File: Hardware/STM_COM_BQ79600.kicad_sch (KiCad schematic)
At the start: 8 parts, among them U3 PBQ79600PWQ1

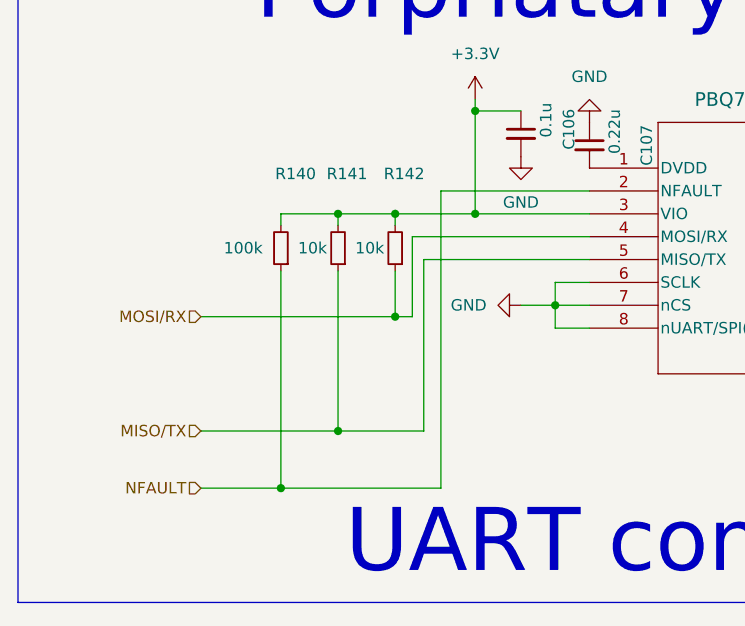
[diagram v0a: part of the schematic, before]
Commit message: Bms plug and play, 2nd iteration with the same pinout
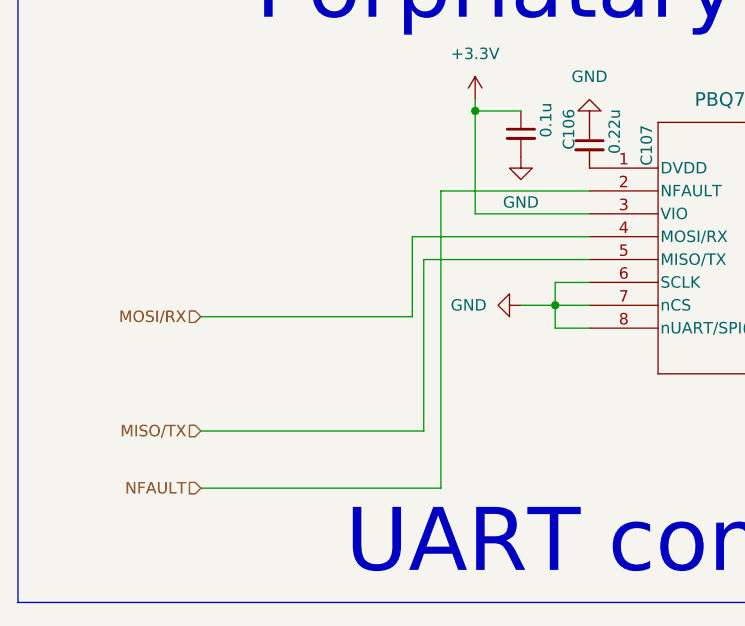
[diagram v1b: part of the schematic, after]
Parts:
- removed R140: 100k, Resistor_SMD:R_0603_1608Metric_Pad0.98x0.95mm_HandSolder, symbol Device:R_Small
- removed R141, R142: 10k, Resistor_SMD:R_0603_1608Metric_Pad0.98x0.95mm_HandSolder, symbol Device:R_Small

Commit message: New connectors jst_xh for low voltage side of bms
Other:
- title: (none) -> Battery Management System for a high power gokart battery
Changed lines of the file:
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@@
 	(generator_version "10.0")
 	(paper "A4")
+	(title_block
+		(title "Battery Management System for a high power gokart battery")
+	)
 	(rectangle
 		(start 53.34 45.72)
